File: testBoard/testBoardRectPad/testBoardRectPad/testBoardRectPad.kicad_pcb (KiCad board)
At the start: 2 copper layers, 2 parts

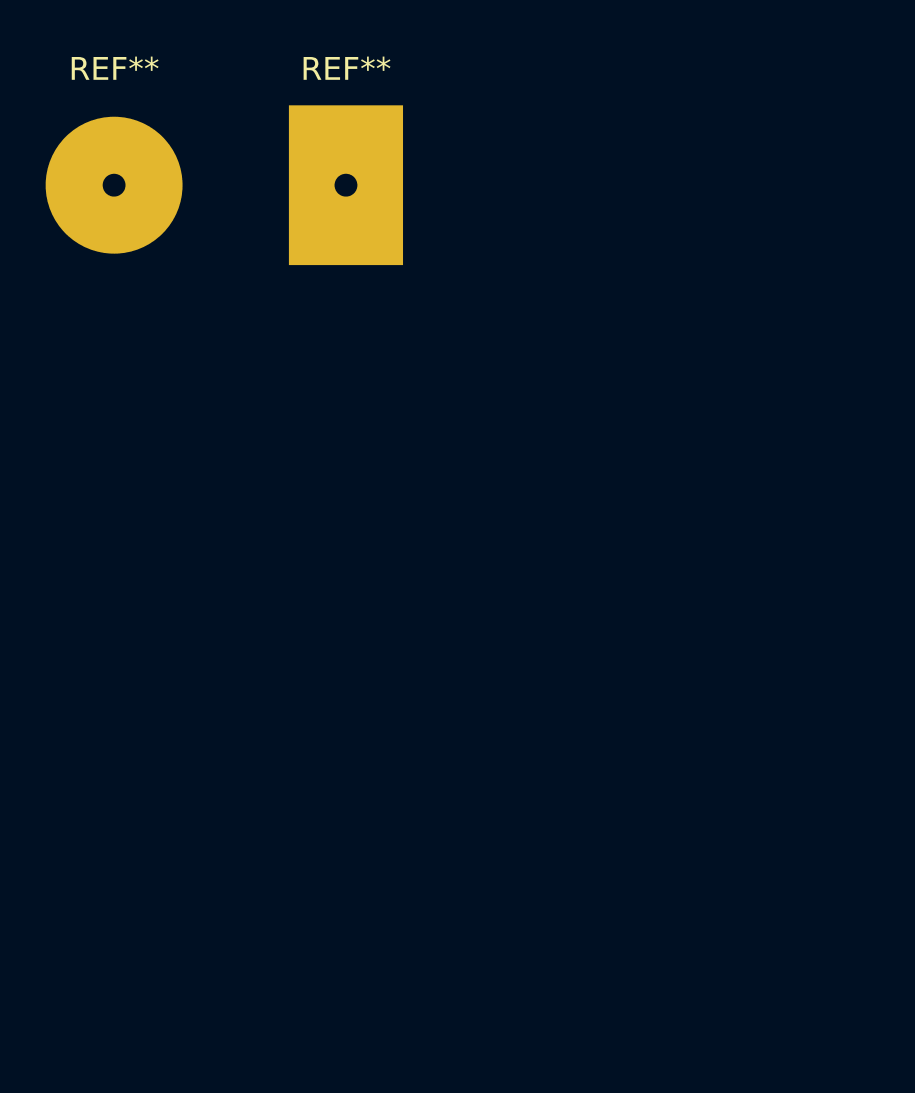
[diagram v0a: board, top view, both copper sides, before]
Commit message: Absolute and relation coordinates in soft parser G-code.
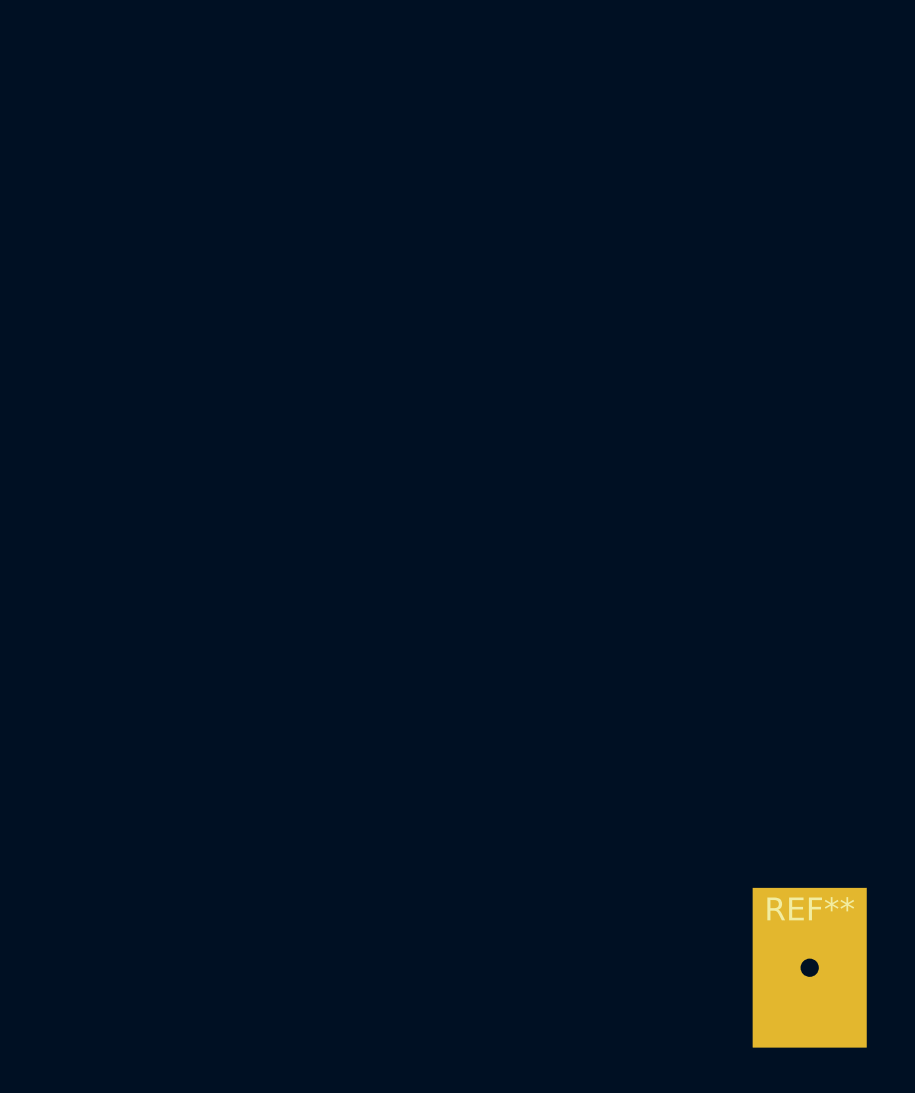
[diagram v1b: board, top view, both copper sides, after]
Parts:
- removed the REF** at (85.1, 45.7)
- removed the REF** at (74.9, 45.7)
- added REF**: SolderWirePad_1x01_Drill0.8mm, Connector_Wire:SolderWirePad_1x01_Drill0.8mm, F.Cu at (105.4, 80.0)
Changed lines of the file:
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@@
     (tracks 0)
     (zones 0)
-    (modules 2)
+    (modules 1)
     (nets 1)
   )
@@
     (mod_text_width 0.15)
     (pad_size 5 7)
-    (pad_drill 1)
+    (pad_drill 0.8001)
     (pad_to_mask_clearance 0.051)
     (solder_mask_min_width 0.25)
     (aux_axis_origin 0 0)
-    (visible_elements 7FFFFFFF)
+    (visible_elements FFFFFF7F)
     (pcbplotparams
-      (layerselection 0x00000_7fffffff)
+      (layerselection 0x010fc_ffffffff)
       (usegerberextensions false)
       (usegerberattributes false)
@@
       (outputformat 1)
       (mirror false)
-      (drillshape 0)
+      (drillshape 1)
       (scaleselection 1)
       (outputdirectory ""))
@@
     (uvia_drill 0.1)
   )
-  (module Connector_Wire:SolderWirePad_1x01_Drill2.5mm (layer F.Cu)
-    (at 85.09 45.72)
+  (module Connector_Wire:SolderWirePad_1x01_Drill0.8mm (layer F.Cu)
+    (at 105.41 80.01)
     (descr "Wire solder connection")
     (tags connector)
     (attr virtual)
-    (fp_text reference REF** (at 0 -5.08) (layer F.SilkS)
+    (fp_text reference REF** (at 0 -2.54) (layer F.SilkS)
       (effects (font (size 1 1) (thickness 0.15)))
     )
-    (fp_text value SolderWirePad_1x01_Drill2.5mm (at 0 5.08) (layer F.Fab)
+    (fp_text value SolderWirePad_1x01_Drill0.8mm (at 0 2.54) (layer F.Fab)
       (effects (font (size 1 1) (thickness 0.15)))
     )
+    (fp_line (start 1.5 1.5) (end -1.5 1.5) (layer F.CrtYd) (width 0.05))
+    (fp_line (start 1.5 1.5) (end 1.5 -1.5) (layer F.CrtYd) (width 0.05))
+    (fp_line (start -1.5 -1.5) (end -1.5 1.5) (layer F.CrtYd) (width 0.05))
+    (fp_line (start -1.5 -1.5) (end 1.5 -1.5) (layer F.CrtYd) (width 0.05))
     (fp_text user %R (at 0 0) (layer F.Fab)
       (effects (font (size 1 1) (thickness 0.15)))
     )
-    (fp_line (start -3.5 -3.5) (end 3.5 -3.5) (layer F.CrtYd) (width 0.05))
-    (fp_line (start -3.5 -3.5) (end -3.5 3.5) (layer F.CrtYd) (width 0.05))
-    (fp_line (start 3.5 3.5) (end 3.5 -3.5) (layer F.CrtYd) (width 0.05))
-    (fp_line (start 3.5 3.5) (end -3.5 3.5) (layer F.CrtYd) (width 0.05))
-    (pad 1 thru_hole rect (at 0 0) (size 5 7) (drill 1) (layers *.Cu *.Mask))
-  )
-  (module Connector_Wire:SolderWirePad_1x01_Drill2.5mm (layer F.Cu)
-    (at 74.93 45.72)
-    (descr "Wire solder connection")
-    (tags connector)
-    (attr virtual)
-    (fp_text reference REF** (at 0 -5.08) (layer F.SilkS)
-      (effects (font (size 1 1) (thickness 0.15)))
-    )
-    (fp_text value SolderWirePad_1x01_Drill2.5mm (at 0 5.08) (layer F.Fab)
-      (effects (font (size 1 1) (thickness 0.15)))
-    )
-    (fp_line (start 3.5 3.5) (end -3.5 3.5) (layer F.CrtYd) (width 0.05))
-    (fp_line (start 3.5 3.5) (end 3.5 -3.5) (layer F.CrtYd) (width 0.05))
-    (fp_line (start -3.5 -3.5) (end -3.5 3.5) (layer F.CrtYd) (width 0.05))
-    (fp_line (start -3.5 -3.5) (end 3.5 -3.5) (layer F.CrtYd) (width 0.05))
-    (fp_text user %R (at 0 0) (layer F.Fab)
-      (effects (font (size 1 1) (thickness 0.15)))
-    )
-    (pad 1 thru_hole circle (at 0 0) (size 5.99948 5.99948) (drill 1) (layers *.Cu *.Mask))
+    (pad 1 thru_hole rect (at 0 0) (size 5 7) (drill 0.8001) (layers *.Cu *.Mask))
   )
 )
